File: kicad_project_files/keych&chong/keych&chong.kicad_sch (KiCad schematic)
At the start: 232 parts, among them J1 USB_C_Receptacle_USB2.0, U1 ATmega32U4-A, Y1 16mhz

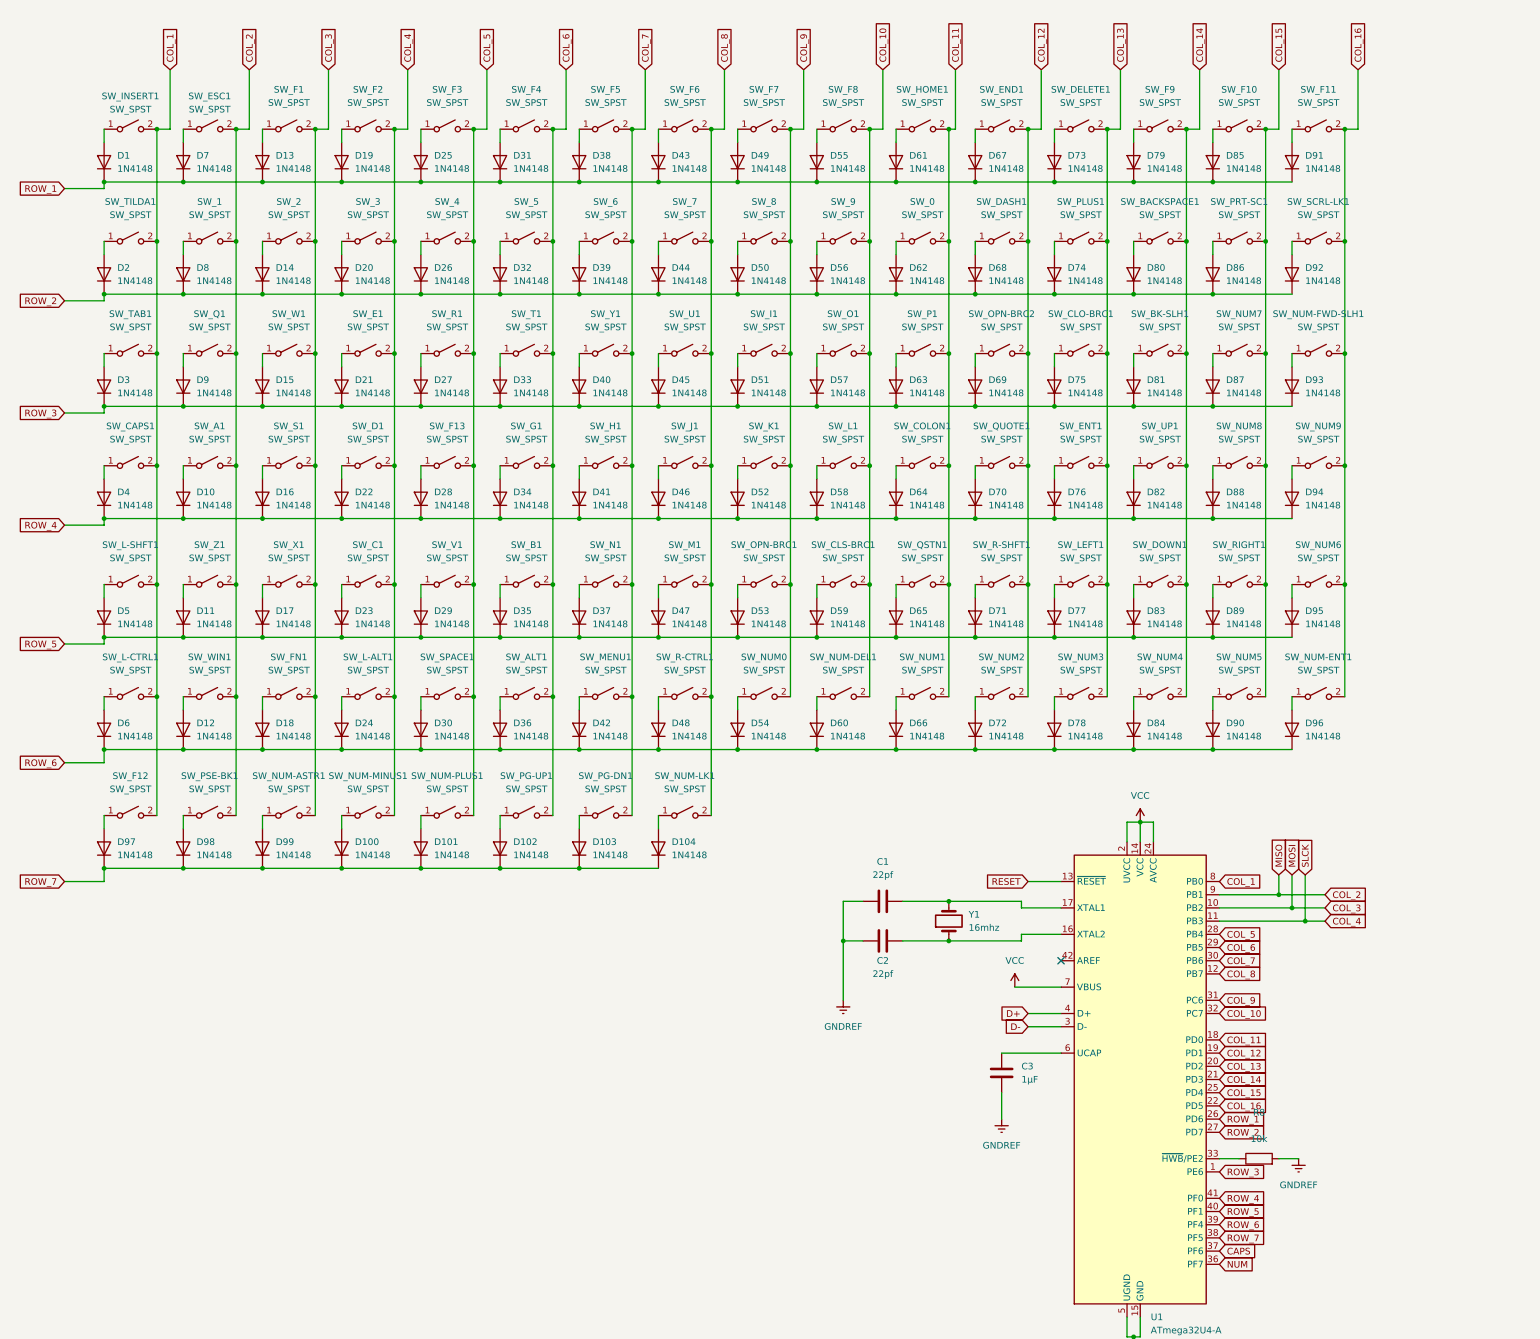
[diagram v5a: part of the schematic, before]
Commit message: update rows and cols
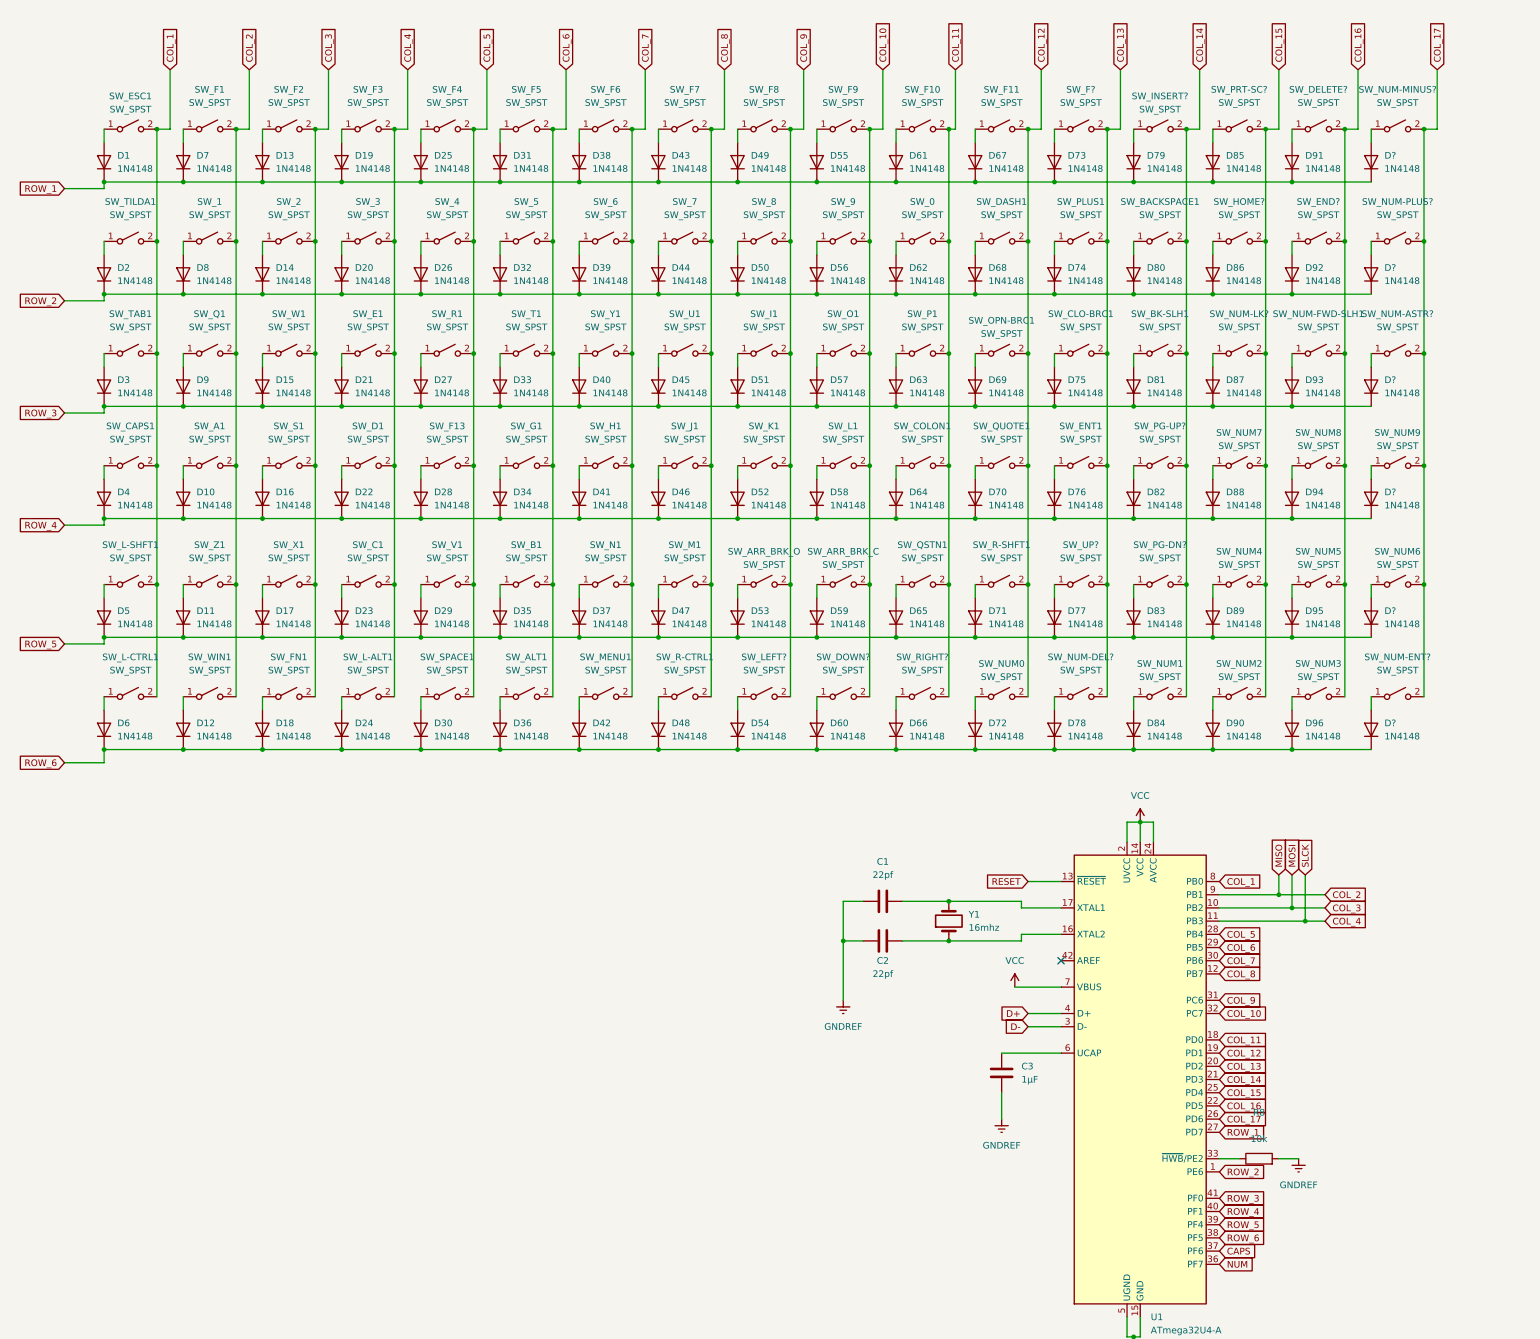
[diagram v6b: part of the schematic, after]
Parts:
- removed D100, D101, D102, D103, D104, D97, D98, D99: 1N4148, Diode_SMD:D_SOD-123, symbol Diode:1N4148
- removed SW_DELETE1, SW_DOWN1, SW_END1, SW_F12, SW_HOME1, SW_INSERT1, SW_LEFT1, SW_NUM-ASTR1, SW_NUM-DEL1, SW_NUM-ENT1, SW_NUM-LK1, SW_NUM-MINUS1, SW_NUM-PLUS1, SW_PG-DN1, SW_PG-UP1, SW_PRT-SC1, SW_PSE-BK1, SW_RIGHT1, SW_SCRL-LK1, SW_UP1: SW_SPST, symbol Switch:SW_SPST
- added D? (x6): 1N4148, Diode_SMD:D_SOD-123, symbol Diode:1N4148
- added SW_DELETE?, SW_DOWN?, SW_END?, SW_F?, SW_HOME?, SW_INSERT?, SW_LEFT?, SW_NUM-ASTR?, SW_NUM-DEL?, SW_NUM-ENT?, SW_NUM-LK?, SW_NUM-MINUS?, SW_NUM-PLUS?, SW_PG-DN?, SW_PG-UP?, SW_PRT-SC?, SW_RIGHT?, SW_UP?: SW_SPST, symbol Switch:SW_SPST
- renumbered SW_CLS-BRC1 to SW_ARR_BRK_C, SW_OPN-BRC1 to SW_ARR_BRK_O, SW_OPN-BRC2 to SW_OPN-BRC1
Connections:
- net ROW_7 is gone; now on net ROW_6: U1.38 (PF5)
- net COL_1: now also SW_ESC1.2 (B)
- net COL_10: now also SW_F9.2 (B), SW_DOWN?.2 (B); no longer SW_F8.2 (B)
- net COL_11: now also SW_F10.2 (B), SW_RIGHT?.2 (B); no longer SW_NUM1.2 (B)
- net COL_12: now also SW_F11.2 (B), SW_NUM0.2 (B); no longer SW_NUM2.2 (B)
- net COL_13: now also SW_F?.2 (B), SW_NUM-DEL?.2 (B), SW_UP?.2 (B); no longer SW_NUM3.2 (B)
- net COL_14: now also SW_NUM1.2 (B), SW_INSERT?.2 (B), SW_PG-DN?.2 (B), SW_PG-UP?.2 (B); no longer SW_F9.2 (B), SW_NUM4.2 (B)
- net COL_15: now also SW_NUM2.2 (B), SW_NUM4.2 (B), SW_HOME?.2 (B), SW_NUM-LK?.2 (B), SW_PRT-SC?.2 (B); no longer SW_F10.2 (B), SW_NUM5.2 (B), SW_NUM8.2 (B)
- net COL_16: now also SW_NUM3.2 (B), SW_NUM5.2 (B), SW_NUM8.2 (B), SW_DELETE?.2 (B), SW_END?.2 (B); no longer SW_F11.2 (B), SW_NUM6.2 (B), SW_NUM9.2 (B)
- net COL_2: now also SW_F1.2 (B); no longer SW_ESC1.2 (B)
- net COL_3: now also SW_F2.2 (B); no longer SW_F1.2 (B)
- net COL_4: now also SW_F3.2 (B); no longer SW_F2.2 (B)
- net COL_5: now also SW_F4.2 (B); no longer SW_F3.2 (B)
- net COL_6: now also SW_F5.2 (B); no longer SW_F4.2 (B)
- net COL_7: now also SW_F6.2 (B); no longer SW_F5.2 (B)
- net COL_8: now also SW_F7.2 (B); no longer SW_F6.2 (B)
- net COL_9: now also SW_F8.2 (B), SW_LEFT?.2 (B); no longer SW_F7.2 (B), SW_NUM0.2 (B)
- net ROW_1: now also U1.27 (PD7), D?.1 (K); no longer U1.26 (PD6)
- net ROW_2: now also U1.1 (PE6), D?.1 (K); no longer U1.27 (PD7)
- net ROW_3: now also U1.41 (PF0), D?.1 (K); no longer U1.1 (PE6)
- net ROW_4: now also U1.40 (PF1), D?.1 (K); no longer U1.41 (PF0)
- net ROW_5: now also U1.39 (PF4), D?.1 (K); no longer U1.40 (PF1)
- net ROW_6: now also D?.1 (K); no longer U1.39 (PF4)
- net at D73.2 (A): now also SW_F?.1 (A)
- net at D92.2 (A): now also SW_END?.1 (A)
- net at D67.2 (A): now also SW_F11.1 (A)
- net at D1.2 (A): now also SW_ESC1.1 (A)
- net at D87.2 (A): now also SW_NUM-LK?.1 (A); no longer SW_NUM7.1 (A)
- net at D38.2 (A): now also SW_F6.1 (A); no longer SW_F5.1 (A)
- net at D78.2 (A): now also SW_NUM-DEL?.1 (A); no longer SW_NUM3.1 (A)
- net at D83.2 (A): now also SW_PG-DN?.1 (A)
- net at D55.2 (A): now also SW_F9.1 (A); no longer SW_F8.1 (A)
- net at D89.2 (A): now also SW_NUM4.1 (A)
- net at D49.2 (A): now also SW_F8.1 (A); no longer SW_F7.1 (A)
- net at D82.2 (A): now also SW_PG-UP?.1 (A)
- net at D31.2 (A): now also SW_F5.1 (A); no longer SW_F4.1 (A)
- net at D66.2 (A): now also SW_RIGHT?.1 (A); no longer SW_NUM1.1 (A)
- net at D43.2 (A): now also SW_F7.1 (A); no longer SW_F6.1 (A)
- net at D77.2 (A): now also SW_UP?.1 (A)
- net at D79.2 (A): now also SW_INSERT?.1 (A); no longer SW_F9.1 (A)
- net at D91.2 (A): now also SW_DELETE?.1 (A); no longer SW_F11.1 (A)
- net at D86.2 (A): now also SW_HOME?.1 (A)
- net at D88.2 (A): now also SW_NUM7.1 (A); no longer SW_NUM8.1 (A)
- net at D60.2 (A): now also SW_DOWN?.1 (A)
- net at SW_NUM2.1 (A): now also D90.2 (A); no longer D72.2 (A)
- net at D19.2 (A): now also SW_F3.1 (A); no longer SW_F2.1 (A)
- net at D13.2 (A): now also SW_F2.1 (A); no longer SW_F1.1 (A)
- net at SW_NUM9.1 (A): now also D?.2 (A); no longer D94.2 (A)
- net at D25.2 (A): now also SW_F4.1 (A); no longer SW_F3.1 (A)
- net at D7.2 (A): now also SW_F1.1 (A); no longer SW_ESC1.1 (A)
- net at SW_NUM6.1 (A): now also D?.2 (A); no longer D95.2 (A)
- net at SW_NUM5.1 (A): now also D95.2 (A); no longer D90.2 (A)
- net at D61.2 (A): now also SW_F10.1 (A)
- net at D85.2 (A): now also SW_PRT-SC?.1 (A); no longer SW_F10.1 (A)
- net at D96.2 (A): now also SW_NUM3.1 (A)
- net at SW_NUM0.1 (A): now also D72.2 (A); no longer D54.2 (A)
- net at D84.2 (A): now also SW_NUM1.1 (A); no longer SW_NUM4.1 (A)
- new net: D?.2 (A), SW_NUM-ASTR?.1 (A)
- new net: D94.2 (A), SW_NUM8.1 (A)
- new net: D?.2 (A), SW_NUM-ENT?.1 (A)
- new net: D?.2 (A), SW_NUM-MINUS?.1 (A)
- new net: D54.2 (A), SW_LEFT?.1 (A)
- new net: D?.2 (A), SW_NUM-PLUS?.1 (A)
- new net COL_17: SW_NUM-ASTR?.2 (B), SW_NUM-ENT?.2 (B), SW_NUM-MINUS?.2 (B), SW_NUM-PLUS?.2 (B), SW_NUM6.2 (B), SW_NUM9.2 (B), U1.26 (PD6)

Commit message: update footprints
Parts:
- gave numbers to parts that had none: 24
- renumbered SW_ARR_BRK_C to SW_ARR_BRK_C1, SW_ARR_BRK_O to SW_ARR_BRK_O1

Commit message: update footprints
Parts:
- D105, D106: footprint (none) -> CLA1A_SMD_LED:CLA1A-WKW-CXAYB153; symbol Device:LED -> CLA1A-WKW-CXAYB153 (SMD_LED):CLA1A-WKW-CXAYB153
- ISCP1: footprint (none) -> Connector_PinHeader_2.00mm:PinHeader_2x03_P2.00mm_Vertical
- R1, R2: footprint (none) -> Resistor_SMD:R_0402_1005Metric_Pad0.72x0.64mm_HandSolder
- SW_0, SW_1, SW_2, SW_3, SW_4, SW_5, SW_6, SW_7, SW_8, SW_9, SW_A1, SW_ALT1, SW_ARR_BRK_C1, SW_ARR_BRK_O1, SW_B1, SW_BACKSPACE1, SW_BK-SLH1, SW_C1, SW_CAPS1, SW_CLO-BRC1, SW_COLON1, SW_D1, SW_DASH1, SW_DELETE1, SW_DOWN1, SW_E1, SW_END1, SW_ENT1, SW_ESC1, SW_F1, SW_F10, SW_F11, SW_F12, SW_F13, SW_F2, SW_F3, SW_F4, SW_F5, SW_F6, SW_F7, SW_F8, SW_F9, SW_FN1, SW_G1, SW_H1, SW_HOME1, SW_I1, SW_INSERT1, SW_J1, SW_K1, SW_L-ALT1, SW_L-CTRL1, SW_L-SHFT1, SW_L1, SW_LEFT1, SW_M1, SW_MENU1, SW_N1, SW_NUM-ASTR1, SW_NUM-DEL1, SW_NUM-ENT1, SW_NUM-FWD-SLH1, SW_NUM-LK1, SW_NUM-MINUS1, SW_NUM-PLUS1, SW_NUM0, SW_NUM1, SW_NUM2, SW_NUM3, SW_NUM4, SW_NUM5, SW_NUM6, SW_NUM7, SW_NUM8, SW_NUM9, SW_O1, SW_OPN-BRC1, SW_P1, SW_PG-DN1, SW_PG-UP1, SW_PLUS1, SW_PRT-SC1, SW_Q1, SW_QSTN1, SW_QUOTE1, SW_R-CTRL1, SW_R-SHFT1, SW_R1, SW_RESET1, SW_RIGHT1, SW_S1, SW_SPACE1, SW_T1, SW_TAB1, SW_TILDA1, SW_U1, SW_UP1, SW_V1, SW_W1, SW_WIN1, SW_X1, SW_Y1, SW_Z1: footprint (none) -> Button_Switch_Keyboard:SW_Cherry_MX_1.00u_Plate
- U1: footprint Package_QFP:TQFP-44_10x10mm_P0.8mm -> ATMEGA32U4RC-AU:ATMEGA32U4RC-AU
- Y1: footprint (none) -> Crystal:Crystal_HC49-4H_Vertical
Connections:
- net at D105.2, R1.2: now also D105.1
- net at D106.2, R2.2: now also D106.1
- net GNDREF renamed GND
- net GND: now also D105.3, D105.4, D106.3, D106.4; no longer D105.1 (K), D106.1 (K)
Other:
- moved on the sheet: R1, R2
